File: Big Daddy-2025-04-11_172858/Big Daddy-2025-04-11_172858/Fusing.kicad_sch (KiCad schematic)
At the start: 30 parts, among them K1 T9VV1K15-12S, Q3 IXFH34N65X2, Q4 IXFH34N65X2, U11 LM5050-1, U12 LM5050-1, U14 LM317_TO-263, U4 LT1528CQ#PBF

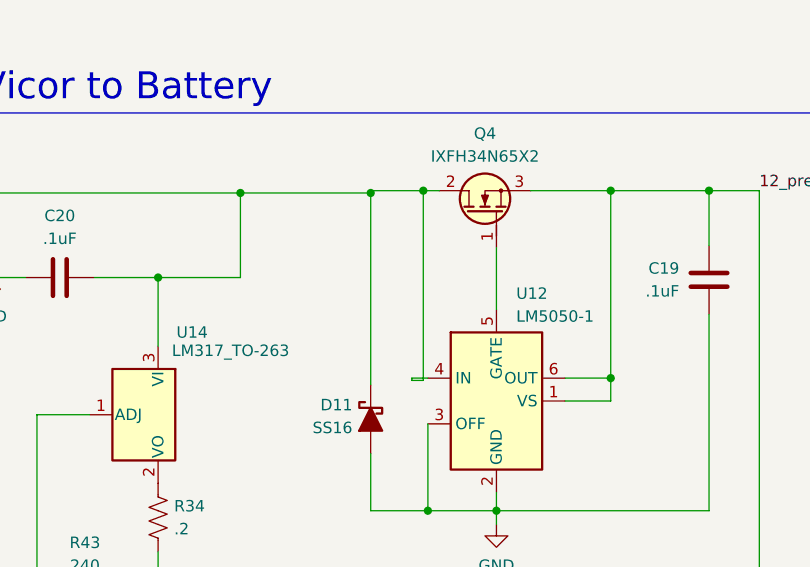
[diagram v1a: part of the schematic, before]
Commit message: PCB fixes
BMS relay
C12 footprint
TSMP resistor connections
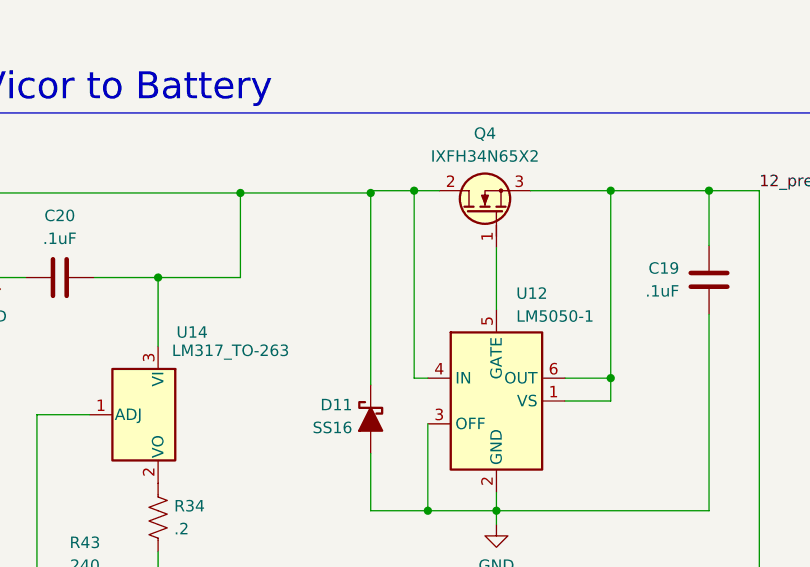
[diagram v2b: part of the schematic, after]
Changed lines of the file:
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@@
+	)
+	(junction
+		(at 107.442 94.234)
+		(diameter 0)
+		(color 0 0 0 0)
 	)
 	(junction
@@
 	(junction
 		(at 203.2 59.944)
-		(diameter 0)
-		(color 0 0 0 0)
-	)
-	(junction
-		(at 108.458 94.234)
 		(diameter 0)
 		(color 0 0 0 0)
@@
 	(wire
 		(pts
-			(xy 107.188 115.316) (xy 107.188 115.062)
-		)
-		(stroke
-			(width 0)
-			(type default)
-		)
-	)
-	(wire
-		(pts
 			(xy 203.2 66.294) (xy 203.2 72.644)
 		)
@@
 	(wire
 		(pts
-			(xy 102.616 94.234) (xy 108.458 94.234)
+			(xy 102.616 94.234) (xy 107.442 94.234)
 		)
 		(stroke
@@
 	(wire
 		(pts
-			(xy 108.458 94.234) (xy 110.236 94.234)
-		)
-		(stroke
-			(width 0)
-			(type default)
-		)
-	)
-	(wire
-		(pts
 			(xy 182.88 122.682) (xy 189.992 122.682)
 		)
@@
 	(wire
 		(pts
-			(xy 108.458 115.316) (xy 107.188 115.316)
-		)
-		(stroke
-			(width 0)
-			(type default)
-		)
-	)
-	(wire
-		(pts
 			(xy 102.616 123.444) (xy 102.616 129.794)
 		)
@@
 	(wire
 		(pts
-			(xy 108.458 94.234) (xy 108.458 115.316)
+			(xy 107.442 94.234) (xy 107.442 115.062)
 		)
 		(stroke
@@
 	(wire
 		(pts
+			(xy 107.442 94.234) (xy 110.236 94.234)
+		)
+		(stroke
+			(width 0)
+			(type default)
+		)
+	)
+	(wire
+		(pts
 			(xy 116.586 129.794) (xy 116.586 127.762)
 		)
@@
 	(wire
 		(pts
+			(xy 107.442 115.062) (xy 108.966 115.062)
+		)
+		(stroke
+			(width 0)
+			(type default)
+		)
+	)
+	(wire
+		(pts
 			(xy 203.2 78.994) (xy 208.534 78.994)
 		)
@@
 		)
 		(stroke
-			(width 0)
-			(type default)
-		)
-	)
-	(wire
-		(pts
-			(xy 107.188 115.062) (xy 108.966 115.062)
-		)
-		(stroke

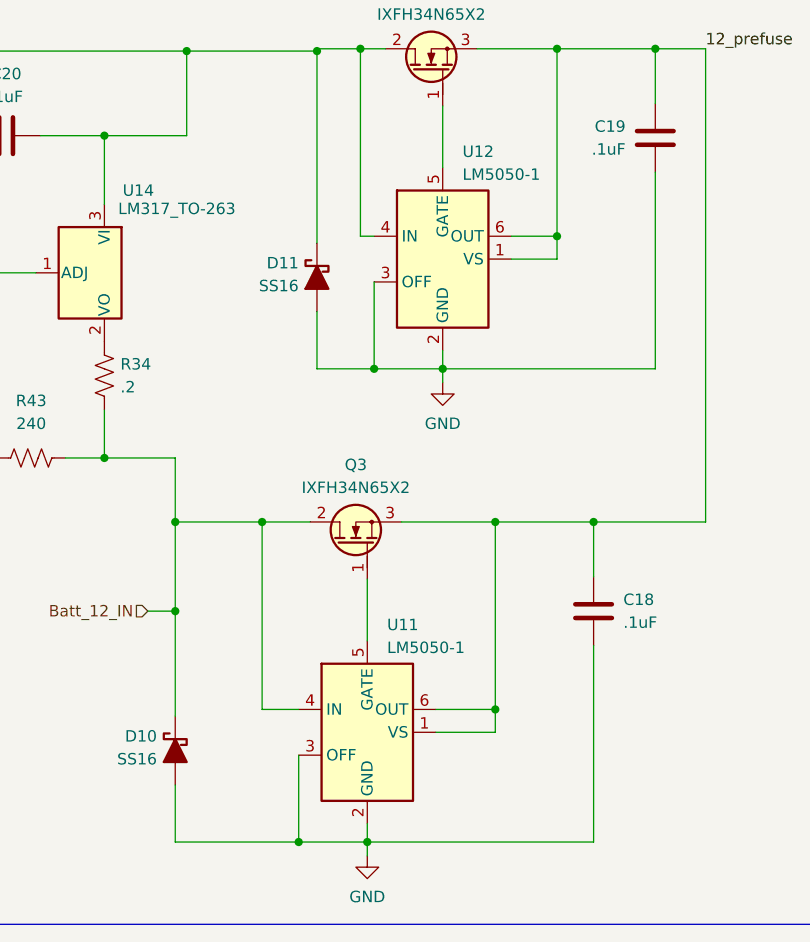
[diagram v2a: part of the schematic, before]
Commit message: BMS Indicator
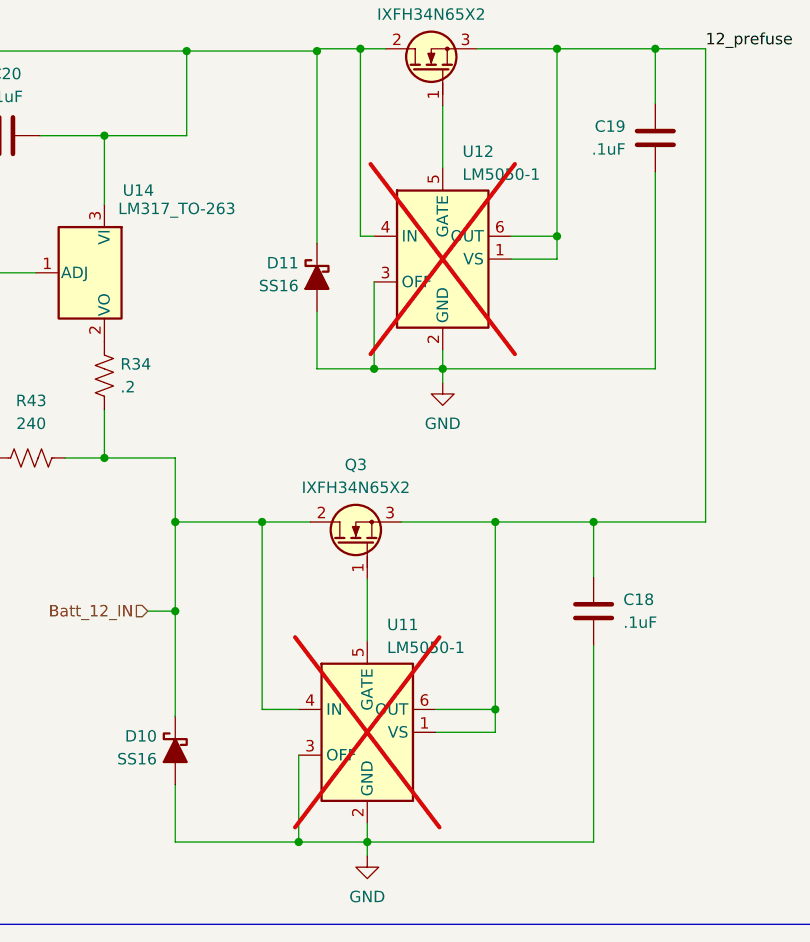
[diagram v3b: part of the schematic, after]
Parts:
- U11, U12: now not fitted
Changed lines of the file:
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@@
 		(in_bom yes)
 		(on_board yes)
-		(dnp no)
+		(dnp yes)
 		(fields_autoplaced yes)
 		(property "Reference" "U11"
@@
 		(in_bom yes)
 		(on_board yes)
-		(dnp no)
+		(dnp yes)
 		(fields_autoplaced yes)
 		(property "Reference" "U12"

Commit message: all the bs
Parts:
- removed C18, C19, C20: .1uF, Capacitor_SMD:C_0603_1608Metric_Pad1.08x0.95mm_HandSolder, symbol Device:C
- removed D10, D11: SS16, Diode_SMD:D_SMA, symbol PCM_Diode_Schottky_AKL:SS16
- removed Q3, Q4: IXFH34N65X2, PCM_Package_TO_SOT_THT_AKL:TO-247-3_Vertical_GDS, symbol PCM_Transistor_MOSFET_AKL:IXFH34N65X2
- removed R34: .2, Resistor_SMD:R_0805_2012Metric_Pad1.20x1.40mm_HandSolder, symbol Device:R_US
- removed R42: 2.4k, Resistor_SMD:R_0603_1608Metric_Pad0.98x0.95mm_HandSolder, symbol Device:R_US
- removed R43: 240, Resistor_SMD:R_0603_1608Metric_Pad0.98x0.95mm_HandSolder, symbol Device:R_US
- removed U11, U12: LM5050-1, Package_TO_SOT_SMD:TSOT-23-6, symbol Power_Management:LM5050-1
- removed U14: LM317_TO-263, Package_TO_SOT_SMD:TO-263-2, symbol Regulator_Linear:LM317_TO-263
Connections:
- net 12_prefuse is gone; now on net Vicor_In: K1.3
- net INT_12V renamed 12V_in
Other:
- note removed: "Charger For Vicor to Battery"
- moved on the sheet: K1
